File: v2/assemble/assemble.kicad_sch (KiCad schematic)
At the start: 96 parts, among them J1 Conn_01x04, SW1 SW_Push, SW10 SW_Push, SW11 SW_Push, SW12 SW_Push, SW13 SW_Push, SW14 SW_Push, SW15 SW_Push, SW16 SW_Push, SW17 SW_Push, SW18 SW_Push, SW19 SW_Push, SW2 SW_Push, SW20 SW_Push, SW21 SW_Push, SW22 SW_Push, SW23 SW_Push, SW24 SW_Push, SW25 SW_Push, SW26 SW_Push, SW27 SW_Push, SW28 SW_Push, SW29 SW_Push, SW3 SW_Push, SW30 SW_Push, SW31 SW_Push, SW32 SW_Push, SW33 SW_Push, SW34 SW_Push, SW35 SW_Push, SW36 SW_Push, SW37 SW_Push, SW38 SW_Push, SW39 SW_Push, SW4 SW_Push, SW40 SW_Push, SW41 SW_Push, SW42 SW_Push, SW44 SW_Push, SW45 RotaryEncoder_Switch, SW46 RotaryEncoder_Switch, SW47 SW_SPDT, SW5 SW_Push, SW6 SW_Push, SW7 SW_Push, SW8 SW_Push, SW9 SW_Push

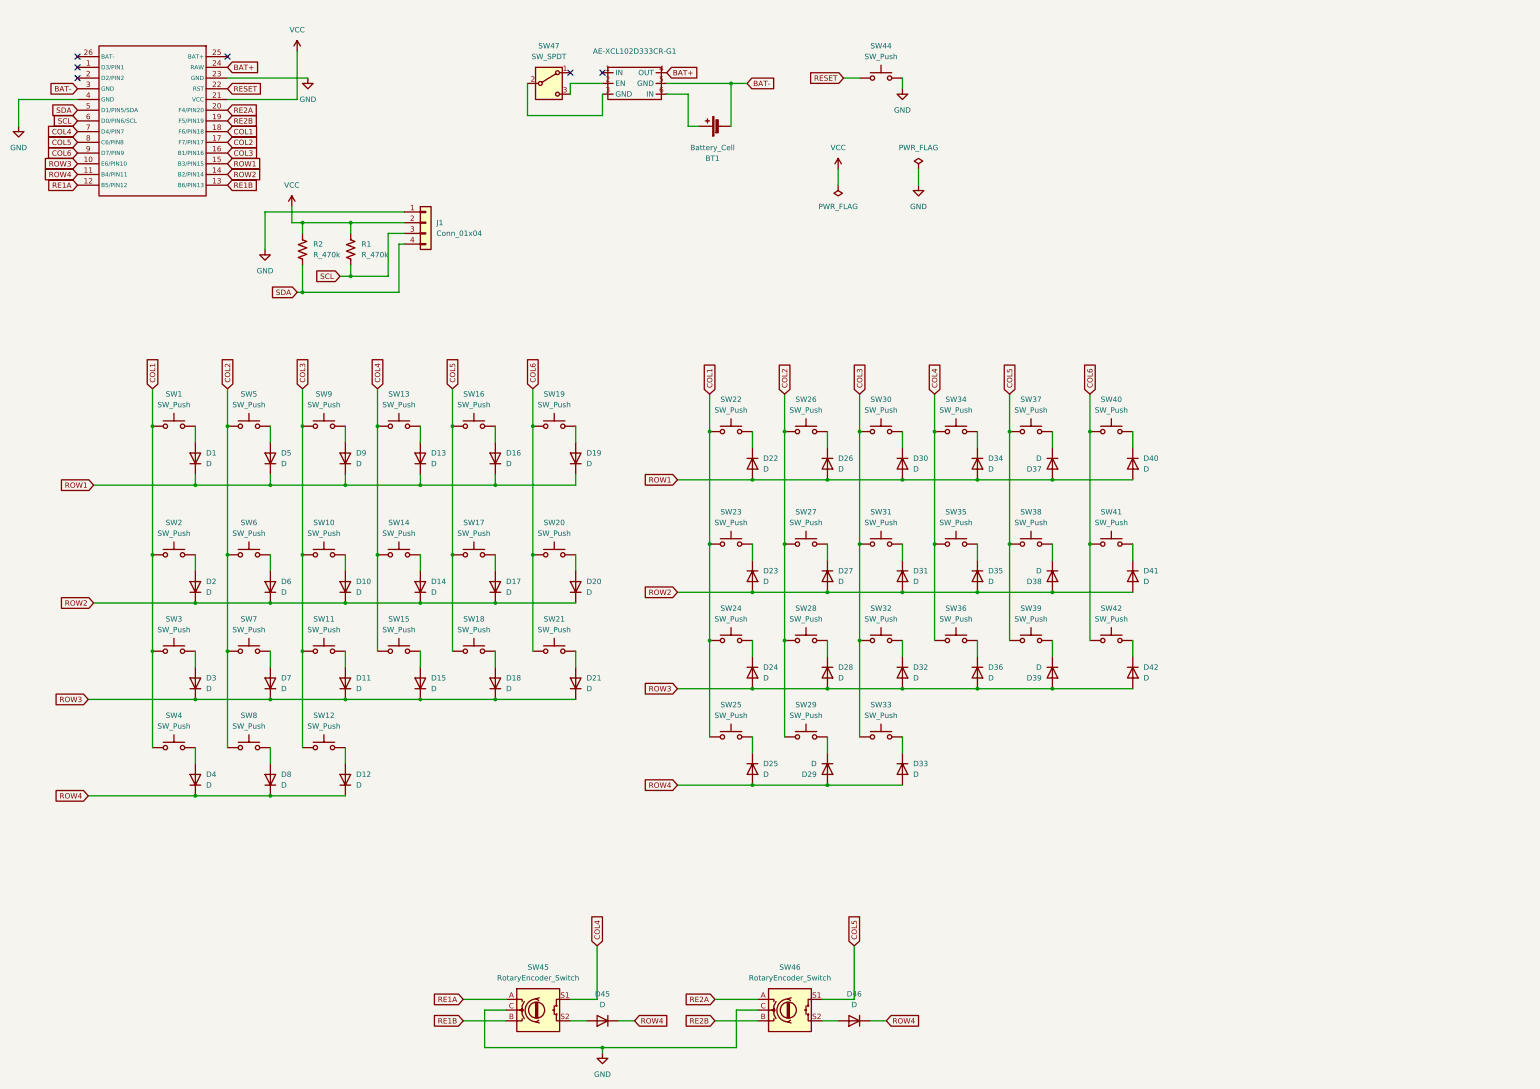
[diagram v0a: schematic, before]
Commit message: feat: implement v2 pcb
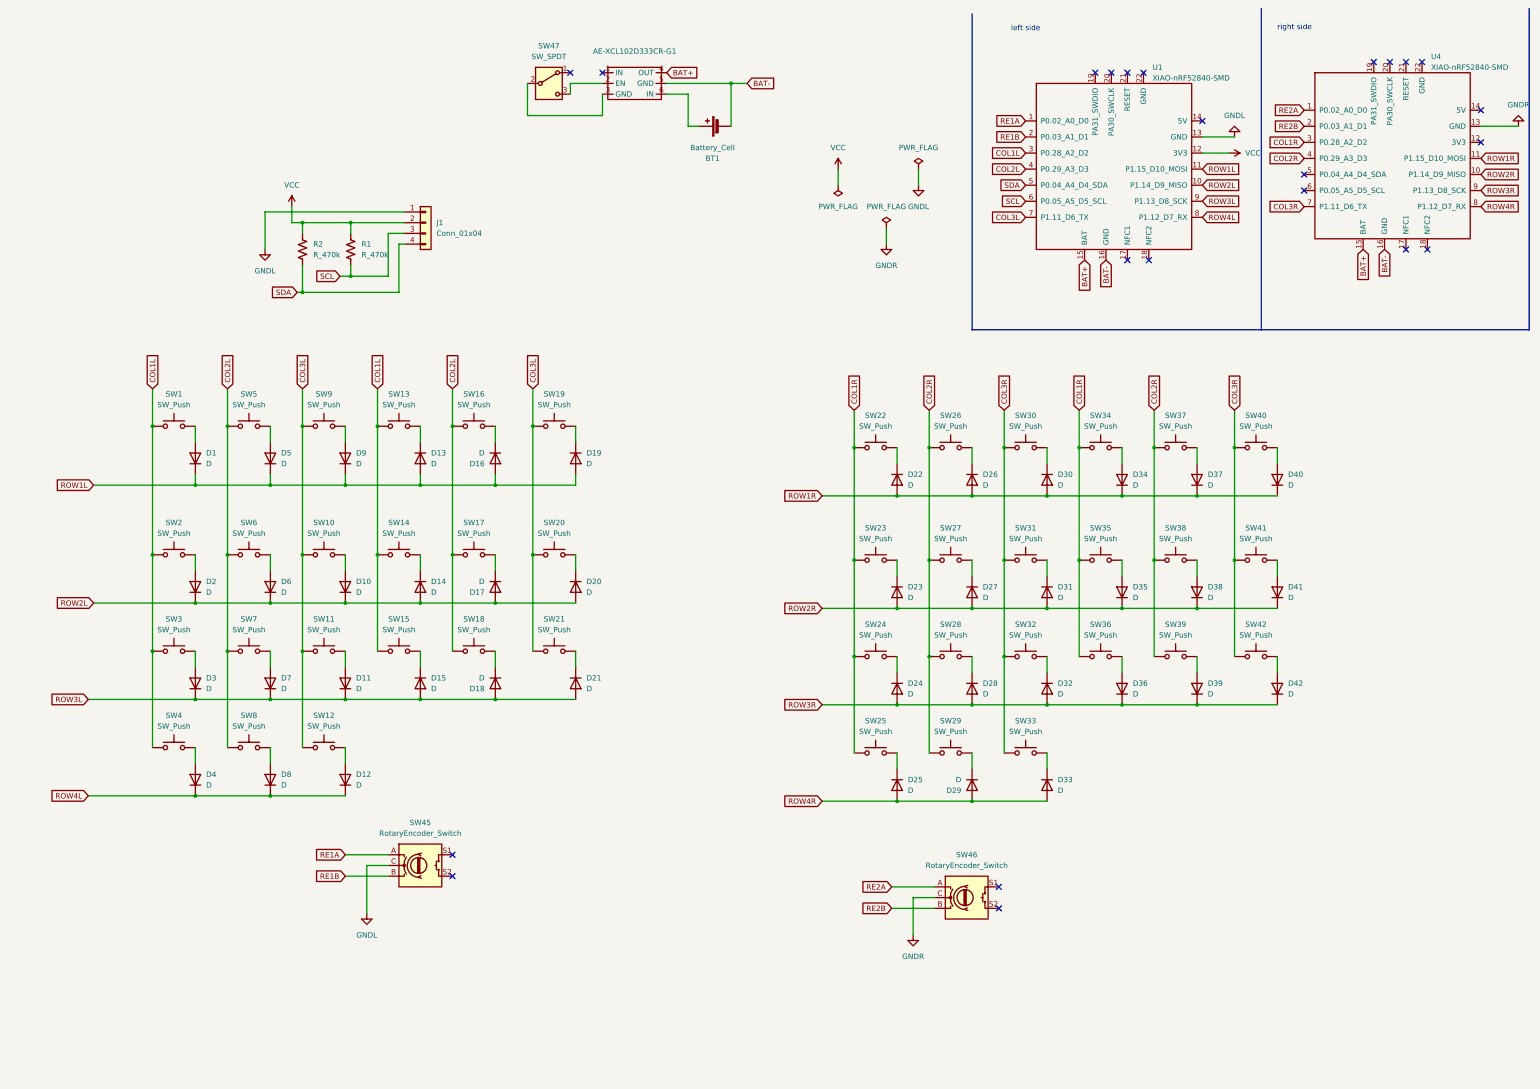
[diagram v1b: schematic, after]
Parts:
- removed D45, D46: D, kbd_Parts:Diode_TH_SMD, symbol Device:D
- removed SW44: SW_Push, kbd_Parts:ResetSW, symbol Switch:SW_Push
- removed U1: ~, kbd_Parts:Micon_BMP_7sKB, symbol kicad-lib:nice!nano v2
- added U1, U4: XIAO-nRF52840-SMD, xiao:XIAO-nRF52840-SMD, symbol xiao:XIAO-nRF52840-SMD
- D1, D10, D11, D12, D13, D14, D15, D16, D17, D18, D19, D2, D20, D21, D22, D23, D24, D25, D26, D27, D28, D29, D3, D30, D31, D32, D33, D34, D35, D36, D37, D38, D39, D4, D40, D41, D42, D5, D6, D7, D8, D9: footprint kbd_Parts:Diode_TH_SMD -> kbd_Parts:Diode_SMD
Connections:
- net BAT+: now also U1.15 (BAT), U4.15 (BAT)
- net BAT-: now also U1.16 (GND), U4.16 (GND)
- net RE1A: now also U1.1 (P0.02_A0_D0)
- net RE1B: now also U1.2 (P0.03_A1_D1)
- net RE2A: now also U4.1 (P0.02_A0_D0)
- net RE2B: now also U4.2 (P0.03_A1_D1)
- net SCL: now also U1.6 (P0.05_A5_D5_SCL)
- net SDA: now also U1.5 (P0.04_A4_D4_SDA)
- net VCC: now also U1.12 (3V3)
- net at SW35.2: now also D35.2 (A); no longer D35.1 (K)
- net at SW37.2: now also D37.2 (A); no longer D37.1 (K)
- net at SW17.2: now also D17.1 (K); no longer D17.2 (A)
- net at SW34.2: now also D34.2 (A); no longer D34.1 (K)
- net at SW36.2: now also D36.2 (A); no longer D36.1 (K)
- net at SW19.2: now also D19.1 (K); no longer D19.2 (A)
- net at SW42.2: now also D42.2 (A); no longer D42.1 (K)
- net at SW15.2: now also D15.1 (K); no longer D15.2 (A)
- net at SW18.2: now also D18.1 (K); no longer D18.2 (A)
- net at SW13.2: now also D13.1 (K); no longer D13.2 (A)
- net at SW20.2: now also D20.1 (K); no longer D20.2 (A)
- net at SW21.2: now also D21.1 (K); no longer D21.2 (A)
- net at SW16.2: now also D16.1 (K); no longer D16.2 (A)
- net at SW38.2: now also D38.2 (A); no longer D38.1 (K)
- net at SW40.2: now also D40.2 (A); no longer D40.1 (K)
- net at SW39.2: now also D39.2 (A); no longer D39.1 (K)
- net at SW41.2: now also D41.2 (A); no longer D41.1 (K)
- net at SW14.2: now also D14.1 (K); no longer D14.2 (A)
- net COL1 renamed COL1L
- net COL1L: now also SW13.1, SW14.1, SW15.1, U1.3 (P0.28_A2_D2); no longer SW22.1, SW23.1, SW24.1, SW25.1
- net COL2 renamed COL2L
- net COL2L: now also SW16.1, SW17.1, SW18.1, U1.4 (P0.29_A3_D3); no longer SW26.1, SW27.1, SW28.1, SW29.1
- net COL3 renamed COL3L
- net COL3L: now also SW19.1, SW20.1, SW21.1, U1.7 (P1.11_D6_TX); no longer SW30.1, SW31.1, SW32.1, SW33.1
- removed net COL4: SW13.1, SW14.1, SW15.1, SW34.1, SW35.1, SW36.1, SW45.S1
- removed net COL5: SW16.1, SW17.1, SW18.1, SW37.1, SW38.1, SW39.1, SW46.S1
- net COL6 renamed COL3R
- net COL3R: now also SW30.1, SW31.1, SW32.1, SW33.1, U4.7 (P1.11_D6_TX); no longer SW19.1, SW20.1, SW21.1
- net GND renamed GNDL
- net GNDL: now also U1.13 (GND); no longer SW46.C
- removed net ROW1: D1.1 (K), D13.1 (K), D16.1 (K), D19.1 (K), D22.2 (A), D26.2 (A), D30.2 (A), D34.2 (A), D37.2 (A), D40.2 (A), D5.1 (K), D9.1 (K)
- removed net ROW2: D10.1 (K), D14.1 (K), D17.1 (K), D2.1 (K), D20.1 (K), D23.2 (A), D27.2 (A), D31.2 (A), D35.2 (A), D38.2 (A), D41.2 (A), D6.1 (K)
- removed net ROW3: D11.1 (K), D15.1 (K), D18.1 (K), D21.1 (K), D24.2 (A), D28.2 (A), D3.1 (K), D32.2 (A), D36.2 (A), D39.2 (A), D42.2 (A), D7.1 (K)
- net ROW4 renamed ROW4L
- net ROW4L: now also U1.8 (P1.12_D7_RX); no longer D25.2 (A), D29.2 (A), D33.2 (A)
- new net COL1R: SW22.1, SW23.1, SW24.1, SW25.1, SW34.1, SW35.1, SW36.1, U4.3 (P0.28_A2_D2)
- new net COL2R: SW26.1, SW27.1, SW28.1, SW29.1, SW37.1, SW38.1, SW39.1, U4.4 (P0.29_A3_D3)
- new net GNDR: SW46.C, U4.13 (GND)
- new net ROW1L: D1.1 (K), D13.2 (A), D16.2 (A), D19.2 (A), D5.1 (K), D9.1 (K), U1.11 (P1.15_D10_MOSI)
- new net ROW1R: D22.2 (A), D26.2 (A), D30.2 (A), D34.1 (K), D37.1 (K), D40.1 (K), U4.11 (P1.15_D10_MOSI)
- new net ROW2L: D10.1 (K), D14.2 (A), D17.2 (A), D2.1 (K), D20.2 (A), D6.1 (K), U1.10 (P1.14_D9_MISO)
- new net ROW2R: D23.2 (A), D27.2 (A), D31.2 (A), D35.1 (K), D38.1 (K), D41.1 (K), U4.10 (P1.14_D9_MISO)
- new net ROW3L: D11.1 (K), D15.2 (A), D18.2 (A), D21.2 (A), D3.1 (K), D7.1 (K), U1.9 (P1.13_D8_SCK)
- new net ROW3R: D24.2 (A), D28.2 (A), D32.2 (A), D36.1 (K), D39.1 (K), D42.1 (K), U4.9 (P1.13_D8_SCK)
- new net ROW4R: D25.2 (A), D29.2 (A), D33.2 (A), U4.8 (P1.12_D7_RX)
- no-connect marks 6 -> 23
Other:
- note added: "left side"
- note added: "right side"
- moved on the sheet: D13, D14, D15, D16, D17, D18, D19, D20, D21, D22, D23, D24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
